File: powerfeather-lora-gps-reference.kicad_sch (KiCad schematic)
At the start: 18 parts, among them J1 Conn_01x05, J11 Conn_01x04, J2 Conn_01x02, J3 Conn_01x04, J4 Conn_01x02, J5 Conn_01x02, J6 Conn_01x04, J7 Conn_01x04, J8 Conn_01x03, J9 Conn_01x03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

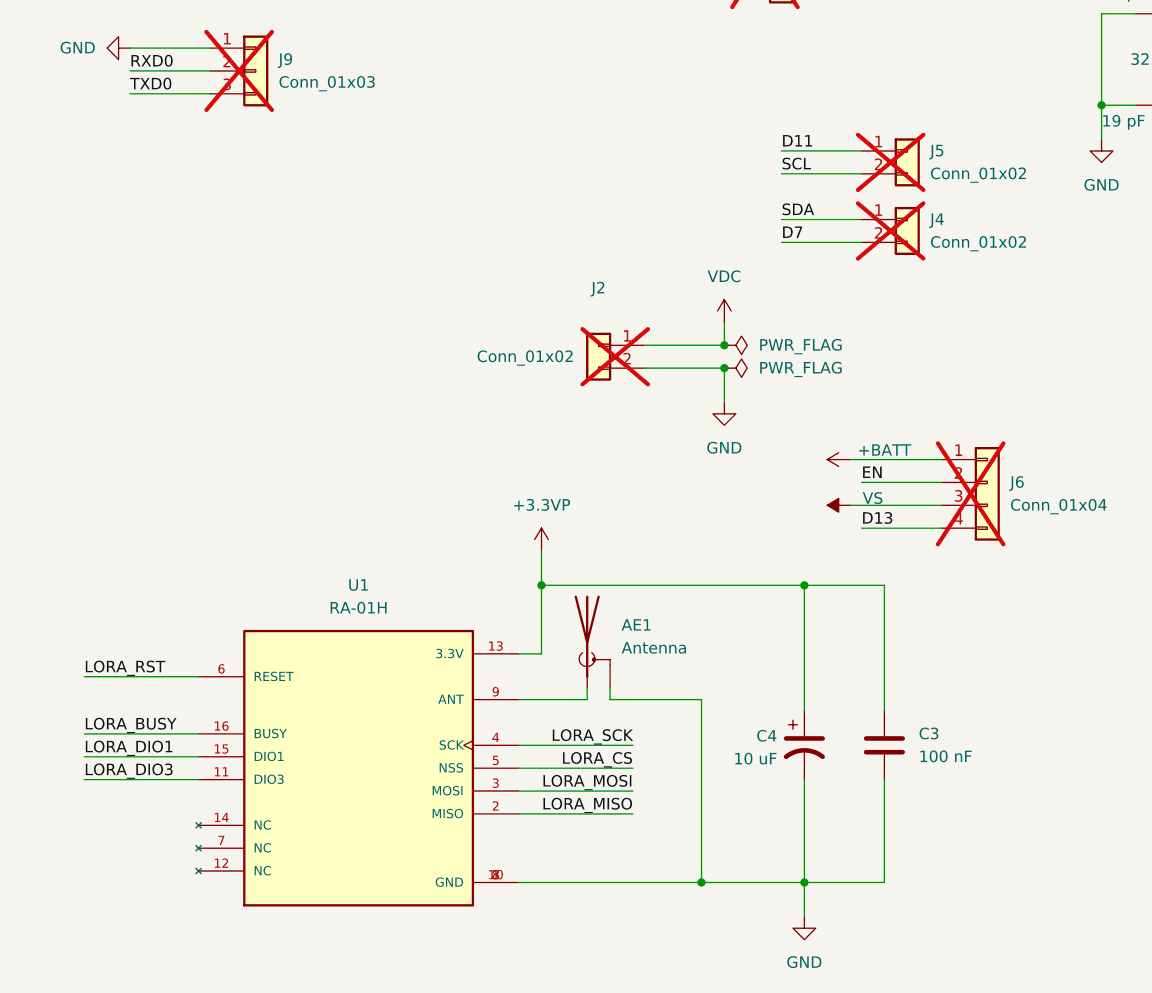
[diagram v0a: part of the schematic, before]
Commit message: Fixes syms and footprints
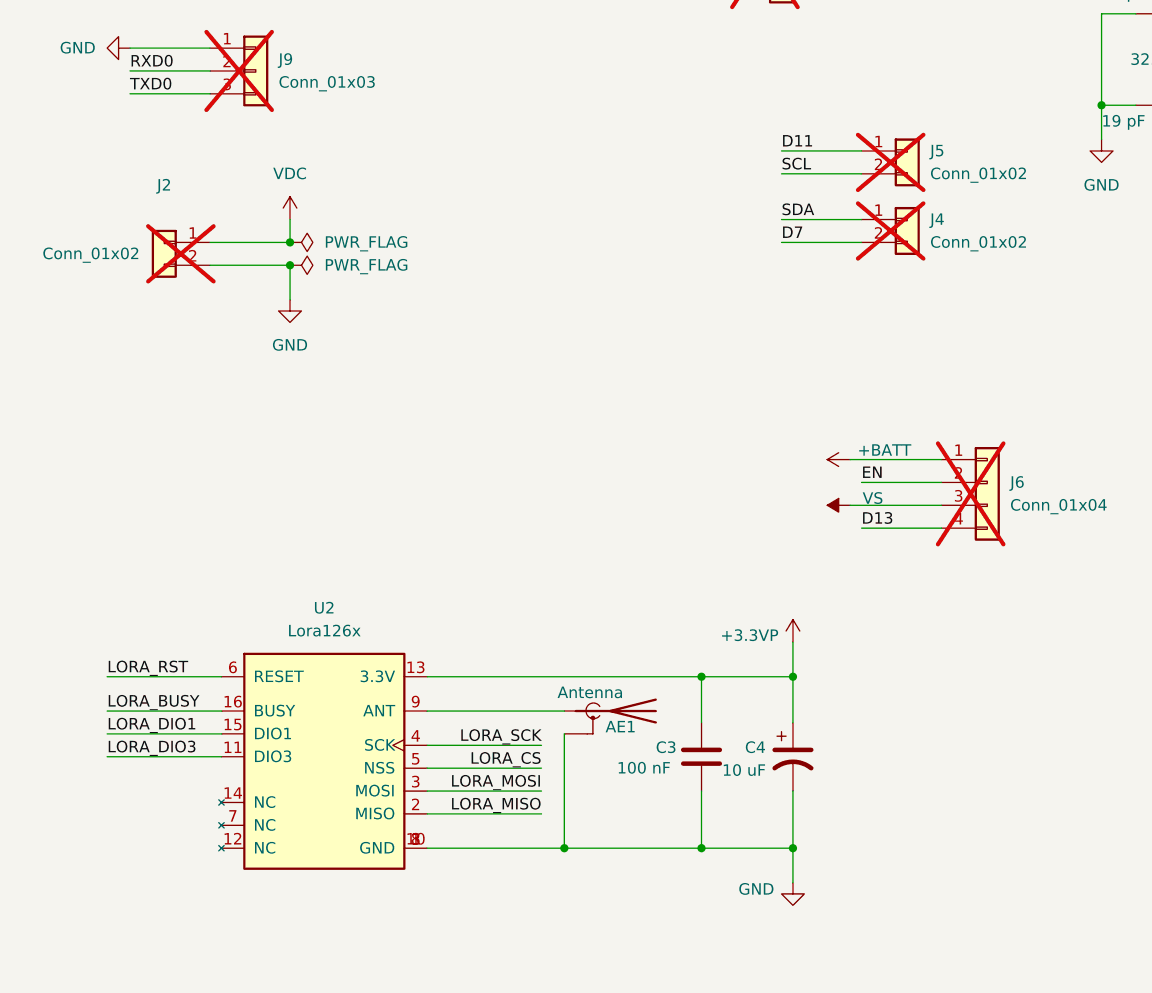
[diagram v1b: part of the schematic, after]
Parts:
- removed U1: RA-01H, PowerFeather_LoRa:Lora126x, symbol PowerFeather_LoRa:Lora126X
- added U2: Lora126x, PowerFeather_LoRa_GPS:Lora126x, symbol PowerFeather_LoRa_GPS:Lora126X
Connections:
- net +3.3VP: now also U2.13 (3.3V)
- net GND: now also U2.1 (GND), U2.10 (GND), U2.8 (GND)
- net LORA_BUSY: now also U2.16 (BUSY)
- net LORA_CS: now also U2.5 (NSS)
- net LORA_DIO1: now also U2.15 (DIO1)
- net LORA_DIO3: now also U2.11 (DIO3)
- net LORA_MISO: now also U2.2 (MISO)
- net LORA_MOSI: now also U2.3 (MOSI)
- net LORA_RST: now also U2.6 (RESET)
- net LORA_SCK: now also U2.4 (SCK)
- net at AE1.1 (A): now also U2.9 (ANT)
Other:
- moved on the sheet: AE1, C3, C4, J2

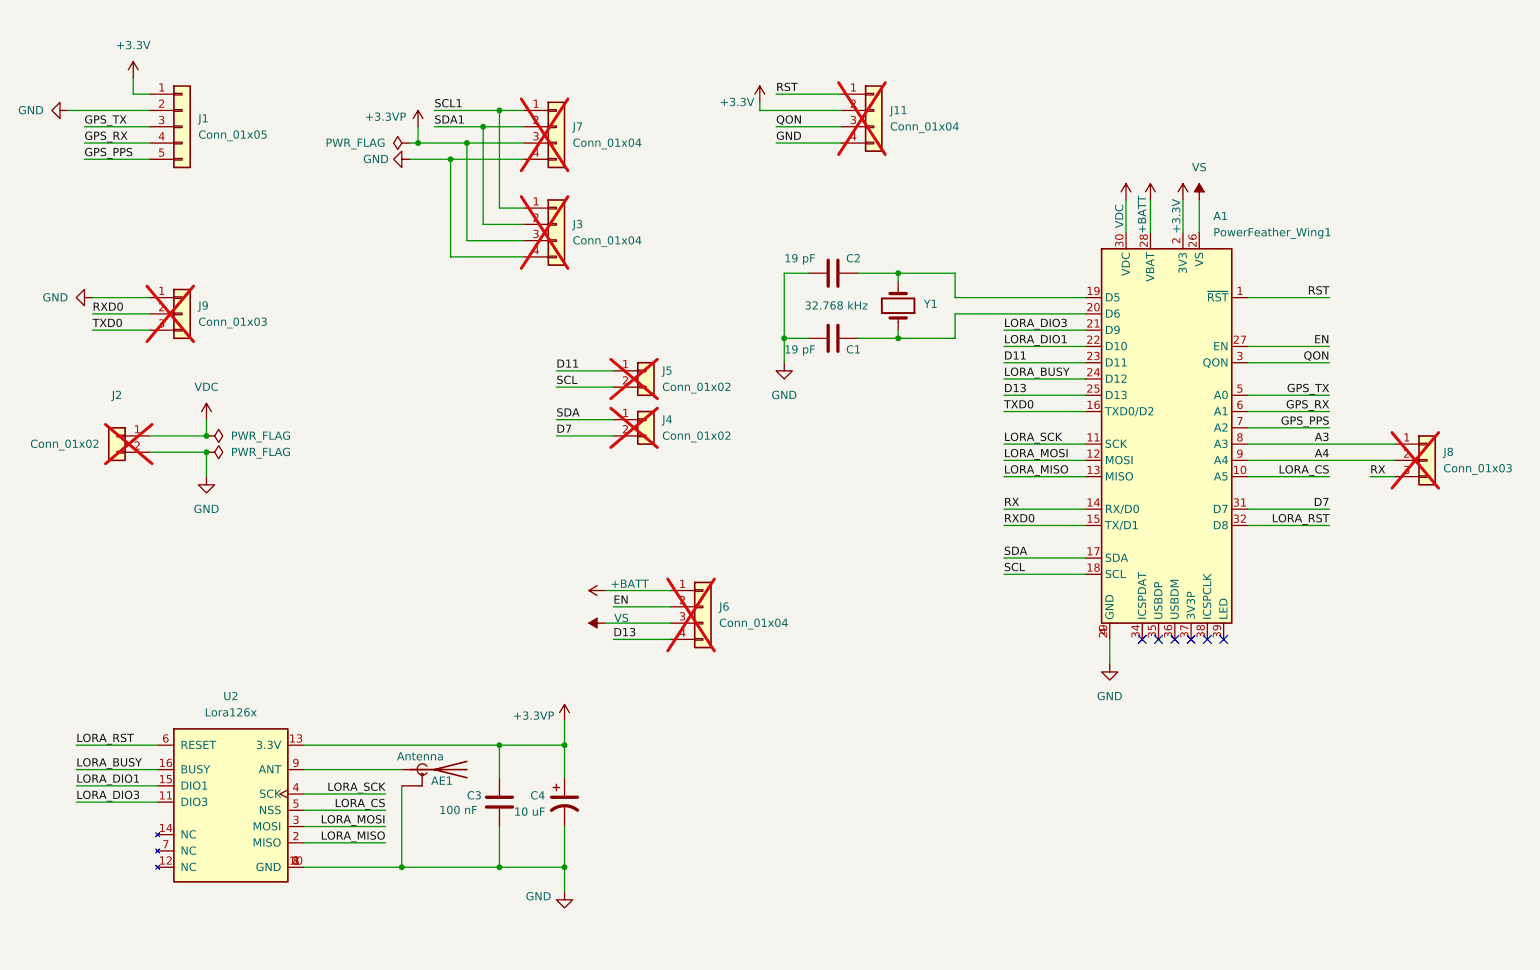
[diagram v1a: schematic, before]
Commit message: Resetting some components for layout
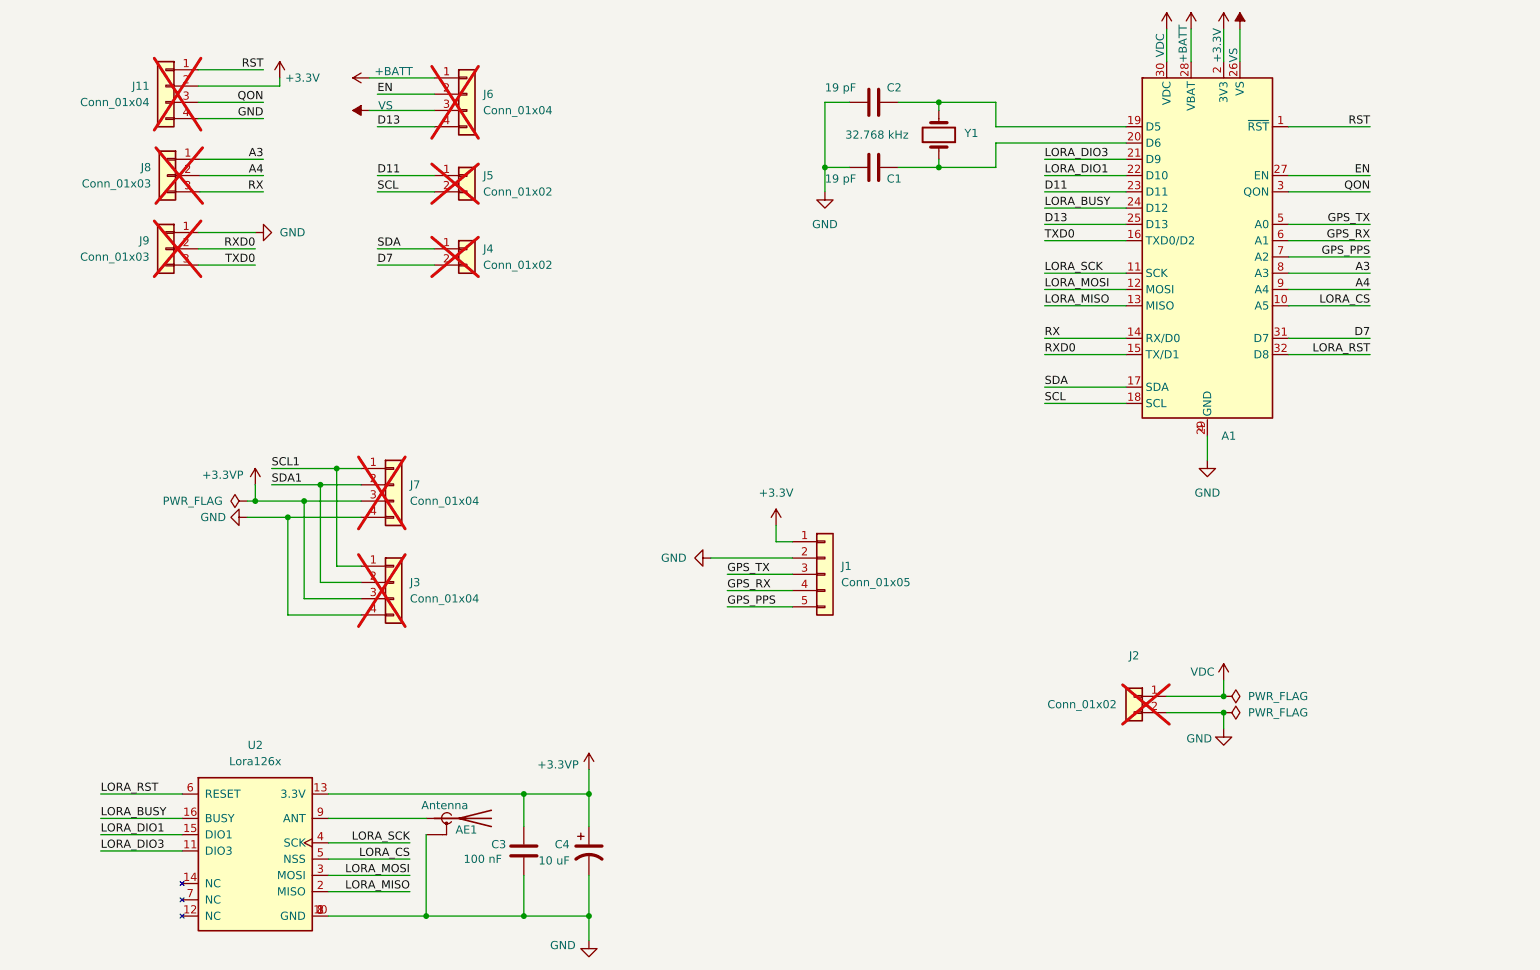
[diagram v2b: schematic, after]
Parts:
- A1: footprint PowerFeather:PowerFeather_Wing1 -> PowerFeather_KiCAD_Lib:PowerFeather_Mainboard; symbol PowerFeather:PowerFeather_Wing1 -> PowerFeather_KiCAD_Lib:PowerFeather_Mainboard
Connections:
- no-connect marks 6 -> 0
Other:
- moved on the sheet: AE1, C1, C2, C3, C4, J1, J11, J2, J3, J4, J5, J6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

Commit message: Rearrange rough layout again
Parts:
- added J10: Conn_01x01, Connector_PinHeader_2.54mm:PinHeader_1x01_P2.54mm_Vertical, symbol Connector_Generic:Conn_01x01
- J3: footprint Connector_PinHeader_2.54mm:PinHeader_1x04_P2.54mm_Vertical -> Connector_PinHeader_1.27mm:PinHeader_1x04_P1.27mm_Vertical
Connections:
- net GND: now also J10.1 (Pin_1)
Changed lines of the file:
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@@
 	(wire
 		(pts
+			(xy 95.25 81.28) (xy 104.14 81.28)
+		)
+		(stroke
+			(width 0)
+			(type default)
+		)
+	)
+	(wire
+		(pts
 			(xy 95.25 58.42) (xy 104.14 58.42)
 		)
@@
 	)
 	(symbol
+		(lib_id "power:GND")
+		(at 95.25 81.28 270)
+		(unit 1)
+		(exclude_from_sim no)
+		(in_bom yes)
+		(on_board yes)
+		(dnp no)
+		(fields_autoplaced yes)
+		(property "Reference" "#PWR012"
+			(at 88.9 81.28 0)
+			(effects
+				(font
+					(size 1.27 1.27)
+				)
+				(hide yes)
+			)
+		)
+		(property "Value" "GND"
+			(at 91.44 81.2799 90)
+			(effects
+				(font
+					(size 1.27 1.27)
+				)
+				(justify right)
+			)
+		)
+		(property "Footprint" ""
+			(at 95.25 81.28 0)
+			(effects
+				(font
+					(size 1.27 1.27)
+				)
+				(hide yes)
+			)
+		)
+		(property "Datasheet" ""
+			(at 95.25 81.28 0)
+			(effects
+				(font
+					(size 1.27 1.27)
+				)
+				(hide yes)
+			)
+		)
+		(property "Description" "Power symbol creates a global label with name \"GND\" , ground"
+			(at 95.25 81.28 0)
+			(effects
+				(font
+					(size 1.27 1.27)
+				)
+				(hide yes)
+			)
+		)
+		(pin "1"
+		)
+		(instances
+			(project ""
+				(path "/2d1d9df7-6bdc-4187-87fe-c5aa58e0b477"
+					(reference "#PWR012")
+					(unit 1)
+				)
+			)
+		)
+	)
+	(symbol
 		(lib_id "power:VDC")
 		(at 218.44 35.56 0)
@@
 			)
 		)
-		(property "Footprint" "Connector_PinHeader_2.54mm:PinHeader_1x04_P2.54mm_Vertical"
+		(property "Footprint" "Connector_PinHeader_1.27mm:PinHeader_1x04_P1.27mm_Vertical"
 			(at 97.79 121.92 0)
 			(effects
@@
 					(unit 1)
 				)
+			)
+		)
+	)
+	(symbol
+		(lib_id "Connector_Generic:Conn_01x01")
+		(at 109.22 81.28 0)
+		(unit 1)
+		(exclude_from_sim no)
+		(in_bom yes)
+		(on_board yes)
+		(dnp yes)
+		(fields_autoplaced yes)
+		(property "Reference" "J10"
+			(at 111.76 80.0099 0)
+			(effects
+				(font
+					(size 1.27 1.27)
+				)
+				(justify left)
+			)
+		)
+		(property "Value" "Conn_01x01"
+			(at 111.76 82.5499 0)
+			(effects
+				(font
+					(size 1.27 1.27)
+				)
+				(justify left)
+			)
+		)
+		(property "Footprint" "Connector_PinHeader_2.54mm:PinHeader_1x01_P2.54mm_Vertical"
+			(at 109.22 81.28 0)
+			(effects
+				(font
+					(size 1.27 1.27)
+				)
+				(hide yes)
+			)
+		)
+		(property "Datasheet" "~"
+			(at 109.22 81.28 0)
+			(effects
+				(font
+					(size 1.27 1.27)
+				)
+				(hide yes)
+			)
+		)
+		(property "Description" "Generic connector, single row, 01x01, script generated (kicad-library-utils/schlib/autogen/connector/)"
+			(at 109.22 81.28 0)
+			(effects
+				(font
+					(size 1.27 1.27)
+				)
+				(hide yes)
+			)
+		)
+		(pin "1"
+		)
+		(instances
+			(project ""
+				(path "/2d1d9df7-6bdc-4187-87fe-c5aa58e0b477"
+					(reference "J10")
+					(unit 1)
+				)

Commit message: Reroute traces
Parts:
- AE1: footprint PowerFeather_LoRa:SMA_Edge -> PowerFeather_LoRa_GPS:SMA_Edge

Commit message: Add page info
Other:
- company: (none) -> PowerFeather
- title: (none) -> DIY LoRa + GPS Wing
